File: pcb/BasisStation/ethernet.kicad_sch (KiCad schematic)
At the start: 2 parts, among them T1 7499011121A, U7 W5500

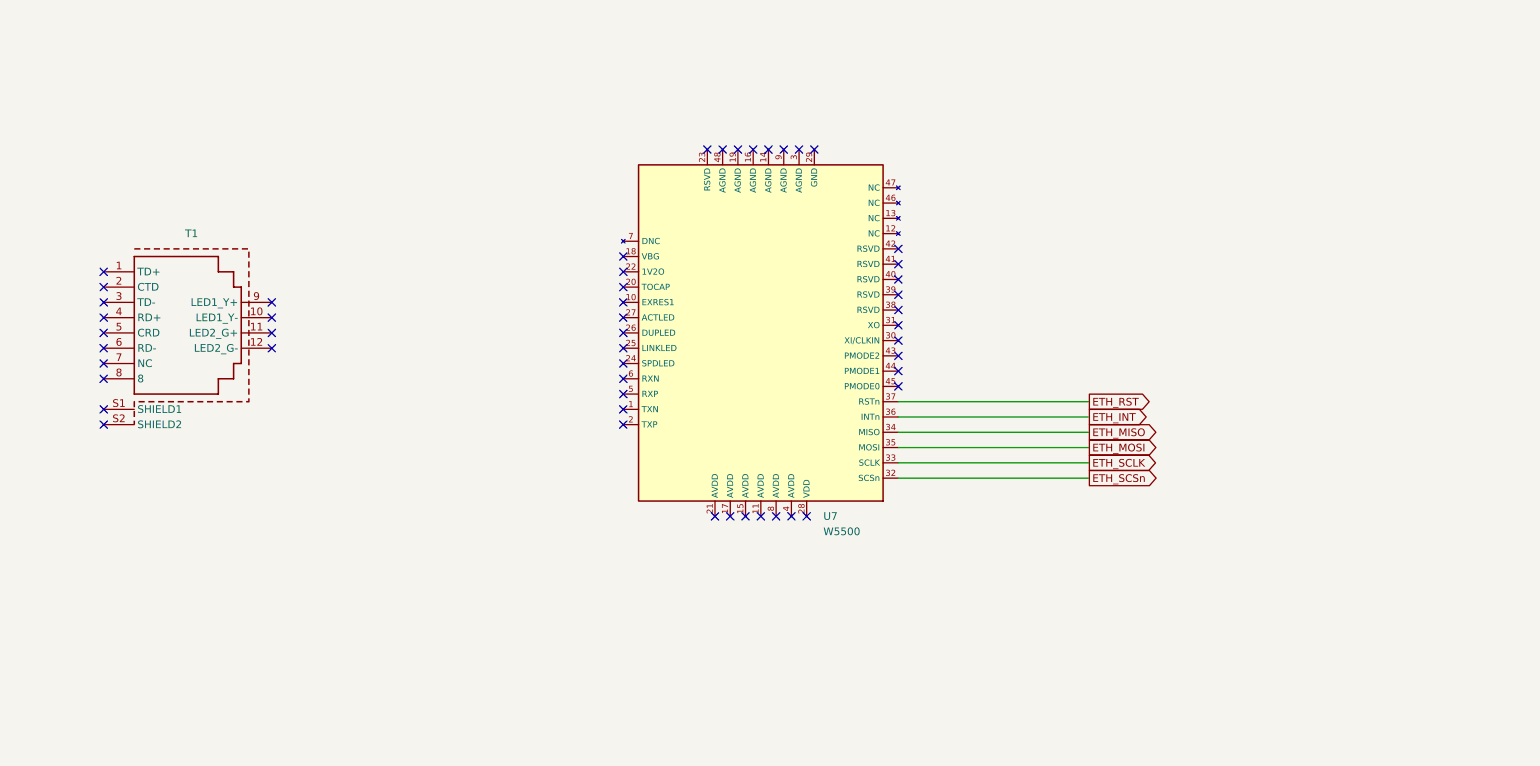
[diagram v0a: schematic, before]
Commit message: v0.00.001 feat(SHBS-5): W5500-Block im Schaltplan vollstaendig beschaltet
Blatt ethernet.kicad_sch mit dem W5500 fertig: Versorgung mit sieben
Abblockkondensatoren je Versorgungspin plus 10-uF-Stuetzkondensator,
analoge Stuetzbeschaltung mit 12,4 kOhm 1% an EXRES1, 4,7 uF an TOCAP
und 10 nF an 1V2O, Taktkreis mit Quarz und zwei 27-pF-Lastkondensatoren,
fuenf Pull-ups an PMODE0-2, INTn und RSTn.

Quarz Y1: Wuerth 830059532 (WE-XTAL, CFPX-104, 25 MHz, CL 18 pF,
+/-20 ppm). Symbol, Footprint und 3D-Modell aus der offiziellen
Wuerth-KiCad-Bibliothek, eigener Bauteilordner, in beiden Lib-Tables
registriert.

Verifikation: alle 29 Pin-Pruefungen gegen die Sollbeschaltung bestanden,
18 Bauteile, Soll und Ist identisch. ERC 0 Fehler und 7 Warnungen, alle
sieben vorbestehend.

Zwei Fehler in der Sollbeschaltung wurden dabei gefunden und korrigiert:
Die Quarzanschluesse sind Pin 1 und 3, nicht 1 und 2 - Pin 2 ist ein
Gehaeusepin, so gezeichnet waere der Oszillator nie angeschwungen. Und
die Lastkondensatoren brauchen 27 pF statt der zunaechst angegebenen
22 pF, weil das Datenblatt CL = 18 pF verlangt.

Co-Authored-By: Claude Opus 5 <noreply@anthropic.com>
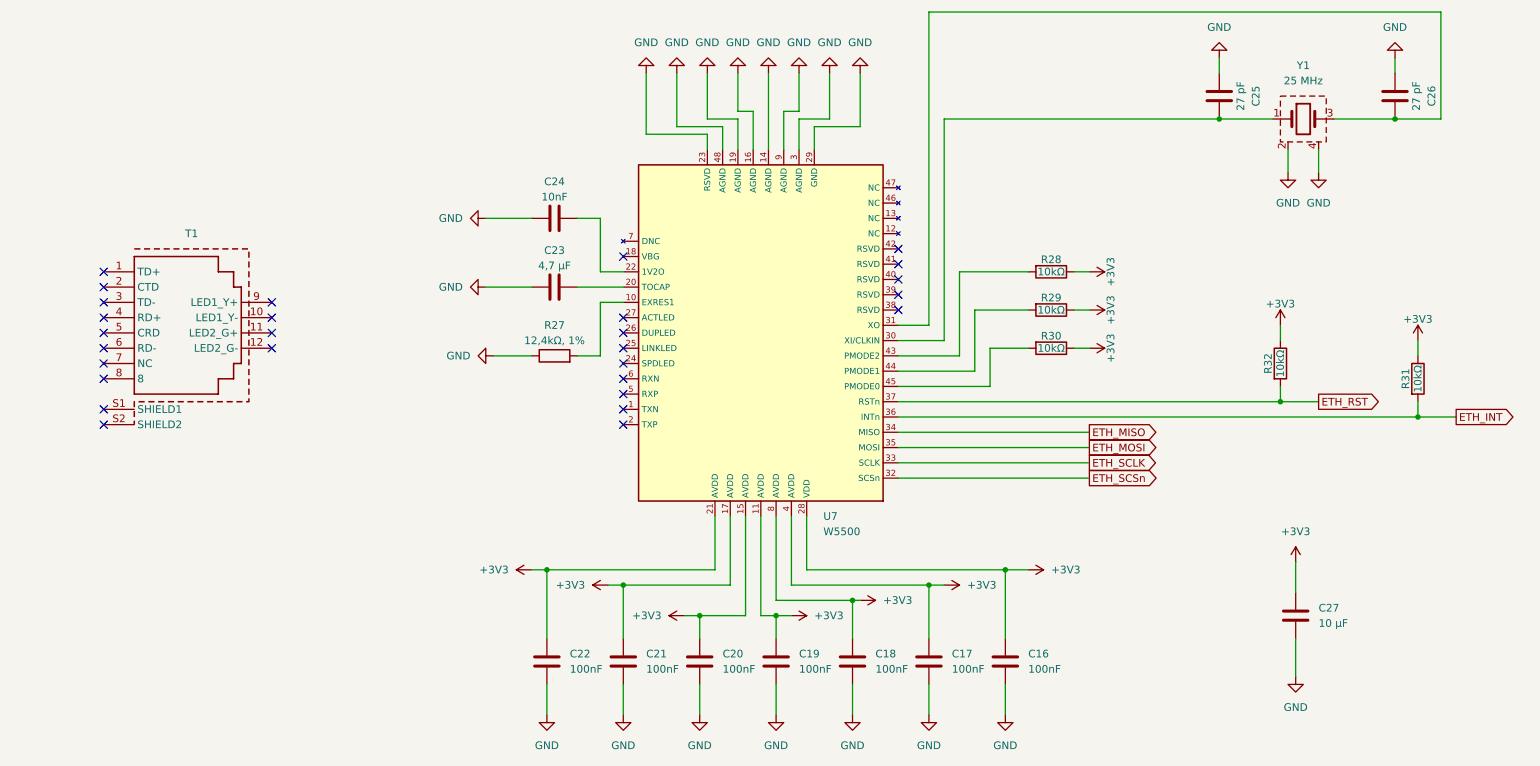
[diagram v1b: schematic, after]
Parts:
- added C16, C17, C18, C19, C20, C21, C22: 100nF, symbol Device:C
- added C23: 4,7 µF, symbol Device:C
- added C24: 10nF, symbol Device:C
- added C25, C26: 27 pF, symbol Device:C
- added C27: 10 µF, symbol Device:C
- added R27: 12,4kΩ, 1%, Resistor_SMD:R_0805_2012Metric, symbol Device:R
- added R28, R29, R30, R31, R32: 10kΩ, Resistor_SMD:R_0805_2012Metric, symbol Device:R
- added Y1: 25 MHz, wuerth_830059532:Y_Wurth_WE-XTAL_Quartz-CFPX-104, symbol wuerth_xtal:CFPX-104_830059532
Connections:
- net ETH_INT: now also R31.2
- net ETH_RST: now also R32.2
- net at U7.10 (EXRES1): now also R27.2
- net +3V3: now reaches U7.11 (AVDD)
- net +3V3: now also U7.15 (AVDD), U7.17 (AVDD), U7.21 (AVDD), U7.28 (VDD), U7.4 (AVDD), U7.8 (AVDD), C16.1, C17.1, C18.1, C19.1, C20.1, C21.1, C22.1, C27.1, R28.1, R29.1, R30.1, R31.1, R32.1
- net GND: now reaches U7.14 (AGND)
- net GND: now also U7.16 (AGND), U7.19 (AGND), U7.23 (RSVD), U7.29 (GND), U7.3 (AGND), U7.48 (AGND), U7.9 (AGND), C16.2, C17.2, C18.2, C19.2, C20.2, C21.2, C22.2, C23.1, C24.1, C25.1, C26.1, C27.2, R27.1, Y1.2 (GND), Y1.4 (GND1)
- net at U7.20 (TOCAP): now also C23.2
- net at U7.22 (1V2O): now also C24.2
- net at U7.30 (XI/CLKIN): now also C25.2, Y1.1
- net at U7.31 (XO): now also C26.2, Y1.3
- net at U7.43 (PMODE2): now also R28.2
- net at U7.44 (PMODE1): now also R29.2
- net at U7.45 (PMODE0): now also R30.2
- no-connect marks 51 -> 28

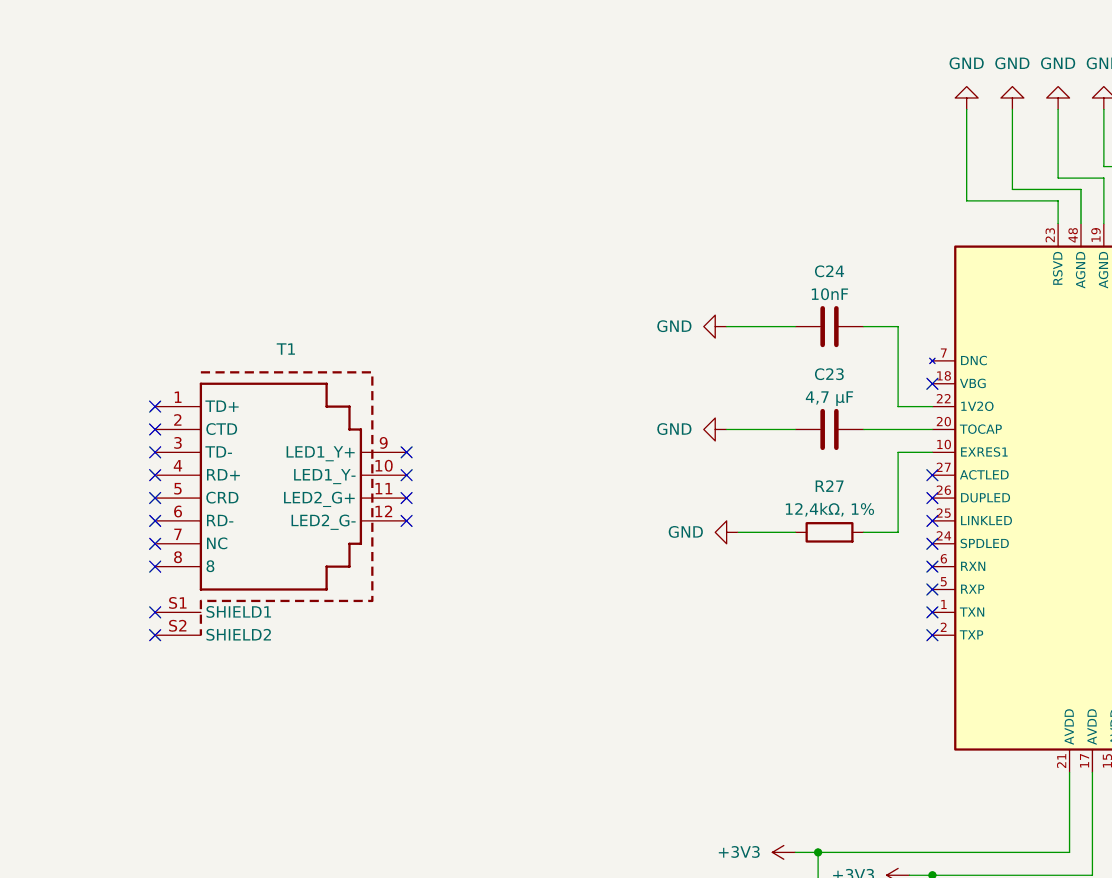
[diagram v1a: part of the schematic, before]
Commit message: v0.00.001 fix(SHBS-5): RX-Pinvertauschung behoben, Schirmung und MDI-Abgleich
Das selbst erstellte W5500-Symbol hatte die Pinnummern von RXN und RXP
vertauscht: Das Datenblatt Rev. 1.0.5 nennt Pin 5 als RXN und Pin 6 als
RXP, im Symbol war es umgekehrt. Wer nach den sichtbaren Pinnamen
verdrahtet, haette das Empfangspaar verpolt - ERC meldet so etwas nie.
Korrigiert durch Tausch der Pinnummern statt der Namen, damit die
bestehende Verdrahtung ohne Umzeichnen richtig wird. Der gecachte
Symbolabzug im Schaltplan wurde gleich mitgezogen.

Schirmung fertiggestellt: T1.S1 und T1.S2 auf ein eigenes Netz CHASSIS,
gekoppelt ueber C28 mit 1 nF/2 kV nach GND, dazu R35 mit 0 Ohm als
unbestueckte Bruecke fuer den EMV-Fall. Der 1-nF-Kondensator hatte
versehentlich dieselbe Referenz wie der 10-uF-Stuetzkondensator bekommen
und heisst jetzt C28.

Abgleich der MDI-Sektion gegen das WIZnet-Referenzschaltbild: Dort sitzen
um die Sende- und Empfangsleitungen Bauteile, die uns fehlen - vier
Abschlusswiderstaende mit 49,9 Ohm, zwei Serienkondensatoren mit 6,8 nF
sowie die Beschaltung der Mittelanzapfungen. Ohne sie stimmt weder die
Leitungsimpedanz noch die Gleichstromtrennung. Analyse in tmp/report/,
Sollbeschaltung in Task 0004 ausformuliert.

Beide Referenzschaltbilder unter pcb/Datasheets/ abgelegt.

Co-Authored-By: Claude Opus 5 <noreply@anthropic.com>
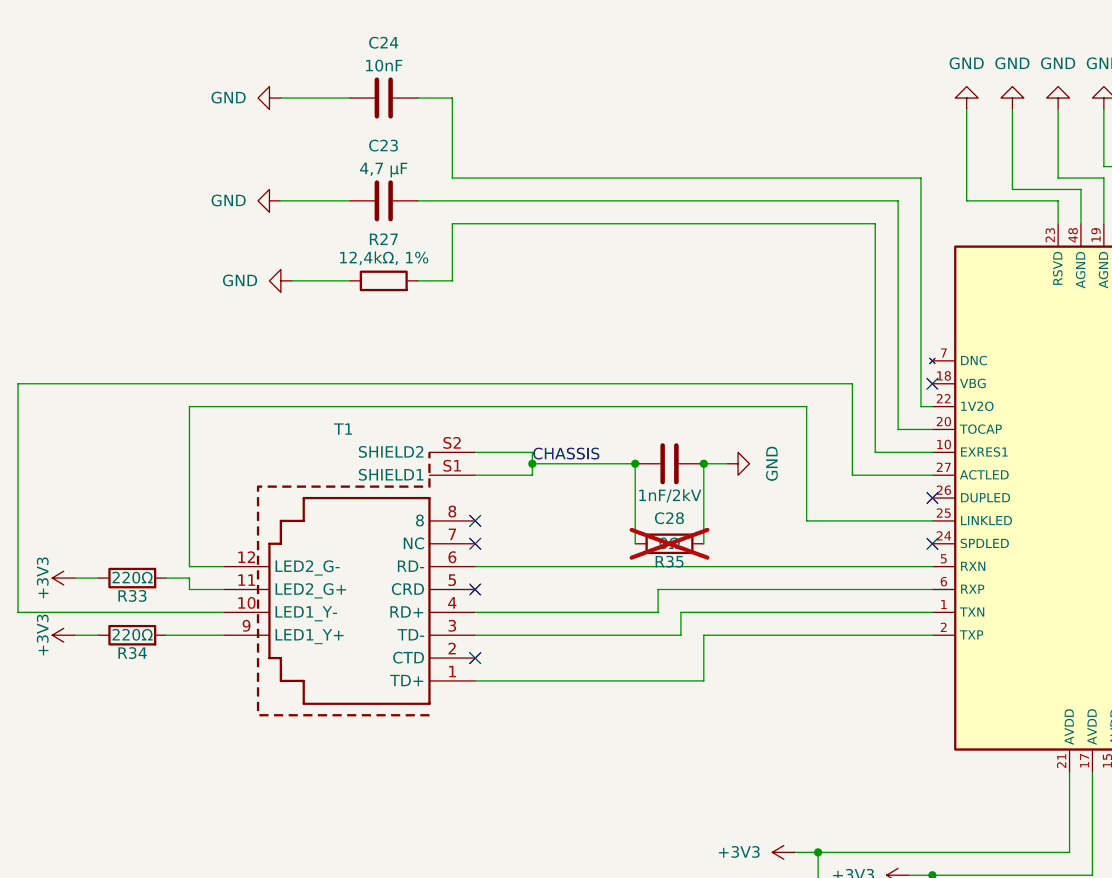
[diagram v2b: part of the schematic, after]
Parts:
- added C28: 1nF/2kV, symbol Device:C
- added R33, R34: 220Ω, Resistor_SMD:R_0805_2012Metric, symbol Device:R
- added R35: 0Ω, Resistor_SMD:R_0805_2012Metric, symbol Device:R
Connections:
- net +3V3: now also R33.1, R34.1
- net GND: now also C28.1, R35.2
- net at U7.1 (TXN): now also T1.3 (TD-)
- net at U7.2 (TXP): now also T1.1 (TD+)
- net at U7.25 (LINKLED): now also T1.12 (LED2_G-)
- net at U7.27 (ACTLED): now also T1.10 (LED1_Y-)
- net at U7.5 (RXN): now also T1.6 (RD-)
- net at U7.6 (RXP): now also T1.4 (RD+)
- net at T1.11 (LED2_G+): now also R33.2
- net at T1.9 (LED1_Y+): now also R34.2
- net CHASSIS: now reaches T1.S1 (SHIELD1)
- net CHASSIS: now also T1.S2 (SHIELD2), C28.2, R35.1
- no-connect marks 28 -> 12
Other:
- moved on the sheet: C23, C24, R27, T1

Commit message: v0.00.001 feat(SHBS-5): MDI-Abschluss und getrennte Analogversorgung gezeichnet
Ethernet-Blatt vervollstaendigt. Neun Bauteile fuer den MDI-Abschluss nach
dem WIZnet-Referenzschaltbild: vier Abschlusswiderstaende mit 49,9 Ohm an
den Sende- und Empfangsleitungen, zwei Serienkondensatoren mit 6,8 nF zur
Gleichstromtrennung im Empfangszweig, dazu 10 Ohm und 22 nF fuer die
gespeiste Sende-Mittelanzapfung sowie 10 nF an der Empfangs-Mittelanzapfung.
Die Mittelanzapfungen haengen ueber lokale Labels TCT und RCT am Stecker,
das spart rund ein Dutzend Leitungskreuzungen.

Versorgung getrennt: +3V3A traegt alle AVDD-Pins samt Abblockung, den
Stuetzkondensator und den TX-Abschluss; +3V3 bleibt fuer VDD, Pull-ups und
LED-Vorwiderstaende. Verbunden ueber FB1.

Gezeichnet durch direkte Bearbeitung der S-Expression, da kein KiCad im
Container verfuegbar ist. Verifikation ueber einen Netz-Tracer, der
Drahtenden, Pin-Positionen, Labels und T-Abzweige auf Drahtmitten
auswertet: alle 29 Pin-Pruefungen bestanden, 35 Bauteile, keine doppelten
Referenzen. ERC 0 Fehler und 7 Warnungen, alle sieben vorbestehend.

Kosmetische Nacharbeit offen: FB1 traegt ein Widerstandssymbol und +3V3A
ist ein lokales Label statt eines Power-Symbols, weil fuer beide offline
keine Symboldefinition verfuegbar war. Netzliste und Footprints stimmen.

Co-Authored-By: Claude Opus 5 <noreply@anthropic.com>
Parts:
- added C29, C30: 6,8nF, Capacitor_SMD:C_0805_2012Metric, symbol Device:C
- added C31: 10nF, Capacitor_SMD:C_0805_2012Metric, symbol Device:C
- added C32: 22nF, Capacitor_SMD:C_0805_2012Metric, symbol Device:C
- added FB1: Ferrit 600R@100MHz, Inductor_SMD:L_0805_2012Metric, symbol Device:R
- added R36, R37, R39, R40: 49,9Ω 1%, Resistor_SMD:R_0805_2012Metric, symbol Device:R
- added R38: 10Ω 1%, Resistor_SMD:R_0805_2012Metric, symbol Device:R
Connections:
- net +3V3: now also FB1.1; no longer C17.1, C18.1, C19.1, C20.1, C21.1, C22.1, C27.1, U7.11 (AVDD), U7.15 (AVDD), U7.17 (AVDD), U7.21 (AVDD), U7.4 (AVDD), U7.8 (AVDD)
- net GND: now also C31.1, C32.2
- net at T1.3 (TD-), U7.1 (TXN): now also R37.1
- net at T1.1 (TD+), U7.2 (TXP): now also R36.1
- net at U7.5 (RXN): now also C30.2, R40.1; no longer T1.6 (RD-)
- net at U7.6 (RXP): now also C29.2, R39.1; no longer T1.4 (RD+)
- net TCT: now reaches T1.2 (CTD)
- net TCT: now also C32.1, R38.1
- net RCT: now reaches T1.5 (CRD)
- net RCT: now also C31.2, R39.2, R40.2
- new net: C29.1, T1.4 (RD+)
- new net: C30.1, T1.6 (RD-)
- new net +3V3A: C17.1, C18.1, C19.1, C20.1, C21.1, C22.1, C27.1, FB1.2, R36.2, R37.2, R38.2, U7.11 (AVDD), U7.15 (AVDD), U7.17 (AVDD), U7.21 (AVDD), U7.4 (AVDD), U7.8 (AVDD)
- no-connect marks 12 -> 10
